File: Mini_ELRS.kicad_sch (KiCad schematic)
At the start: 24 parts, among them J1 Conn_01x06, J2 Conn_01x06, J3 Conn_01x06, SW1 SW_Push, U1 ESP32-PICO-D4, U2 TC2014-3.3VxCTTR, U3 SX1280IMLTRT, Y1 Crystal_GND24_Small

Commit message: update esp32_with_mos
Signed-off-by: huangzzk <huangcmzzk@gmail.com>
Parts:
- removed J1, J2, J3: Conn_01x06, Connector_PinHeader_2.54mm:PinHeader_1x06_P2.54mm_Vertical, symbol Connector_Generic:Conn_01x06
- added J1, J2, J4, J6: Conn_01x03_MountingPin, Connector_Molex:Molex_CLIK-Mate_502386-0370_1x03-1MP_P1.25mm_Horizontal, symbol Connector_Generic_MountingPin:Conn_01x03_MountingPin
- added J3: Conn_01x04, Connector_PinHeader_2.54mm:PinHeader_1x04_P2.54mm_Vertical, symbol Connector_Generic:Conn_01x04
- added J5: Conn_01x03, Connector_Molex:Molex_CLIK-Mate_502386-0370_1x03-1MP_P1.25mm_Horizontal, symbol Connector_Generic:Conn_01x03
- added Q1, Q2: Q_NMOS_GSD, Package_TO_SOT_SMD:SOT-23, symbol Device:Q_NMOS_GSD
- added R4, R5: 10K, Resistor_SMD:R_0402_1005Metric, symbol Device:R
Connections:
- net BUSY: now also U1.5 (SENSOR_VP); no longer U1.34 (IO5)
- net DIO1: now also U1.7 (SENSOR_CAPN); no longer U1.24 (IO4)
- net GND: now also J1.MP (MountPin), J2.MP (MountPin), J3.4 (Pin_4), J4.3 (Pin_3), J4.MP (MountPin), J5.3 (Pin_3), J6.3 (Pin_3), J6.MP (MountPin), Q1.2 (S), Q2.2 (S), R4.2, R5.2
- net LED: now also U1.22 (IO2); no longer U1.35 (IO18)
- net MISO: now also U1.8 (SENSOR_VN); no longer U1.18 (IO12)
- net MOSI: now also U1.16 (IO27); no longer U1.20 (IO13)
- net NRST: now also U1.24 (IO4); no longer U1.22 (IO2)
- net NSS: now also U1.20 (IO13); no longer U1.21 (IO15)
- net RX: now also J3.2 (Pin_2)
- net SCK: now also U1.18 (IO12); no longer U1.17 (IO14)
- net TX: now also J3.3 (Pin_3)
- net PWM5: now reaches U1.28 (SD2/IO9)
- net PWM5: now also J6.1 (Pin_1)
- net PWM7: now reaches U1.12 (IO32)
- net PWM4: now reaches U1.13 (IO33)
- net PWM4: now also J5.1 (Pin_1)
- net PWM3: now reaches U1.14 (IO25)
- net PWM3: now also J4.1 (Pin_1)
- net PWM6: now reaches U1.36 (IO23)
- net PWM1: now reaches U1.39 (IO22)
- net PWM1: now also J1.1 (Pin_1), Q1.1 (G), R4.1
- net PWM8: now reaches U1.42 (IO21)
- net +5V renamed +BATT
- net +BATT: now also J1.2 (Pin_2), J2.2 (Pin_2), J3.1 (Pin_1), J4.2 (Pin_2), J5.2 (Pin_2), J6.2 (Pin_2)
- new net: J2.3 (Pin_3), Q2.3 (D)
- new net: J1.3 (Pin_3), Q1.3 (D)
- new net PWM2: J2.1 (Pin_1), Q2.1 (G), R5.1, U1.34 (IO5)
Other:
- moved on the sheet: AE1, D2, FL1, R3

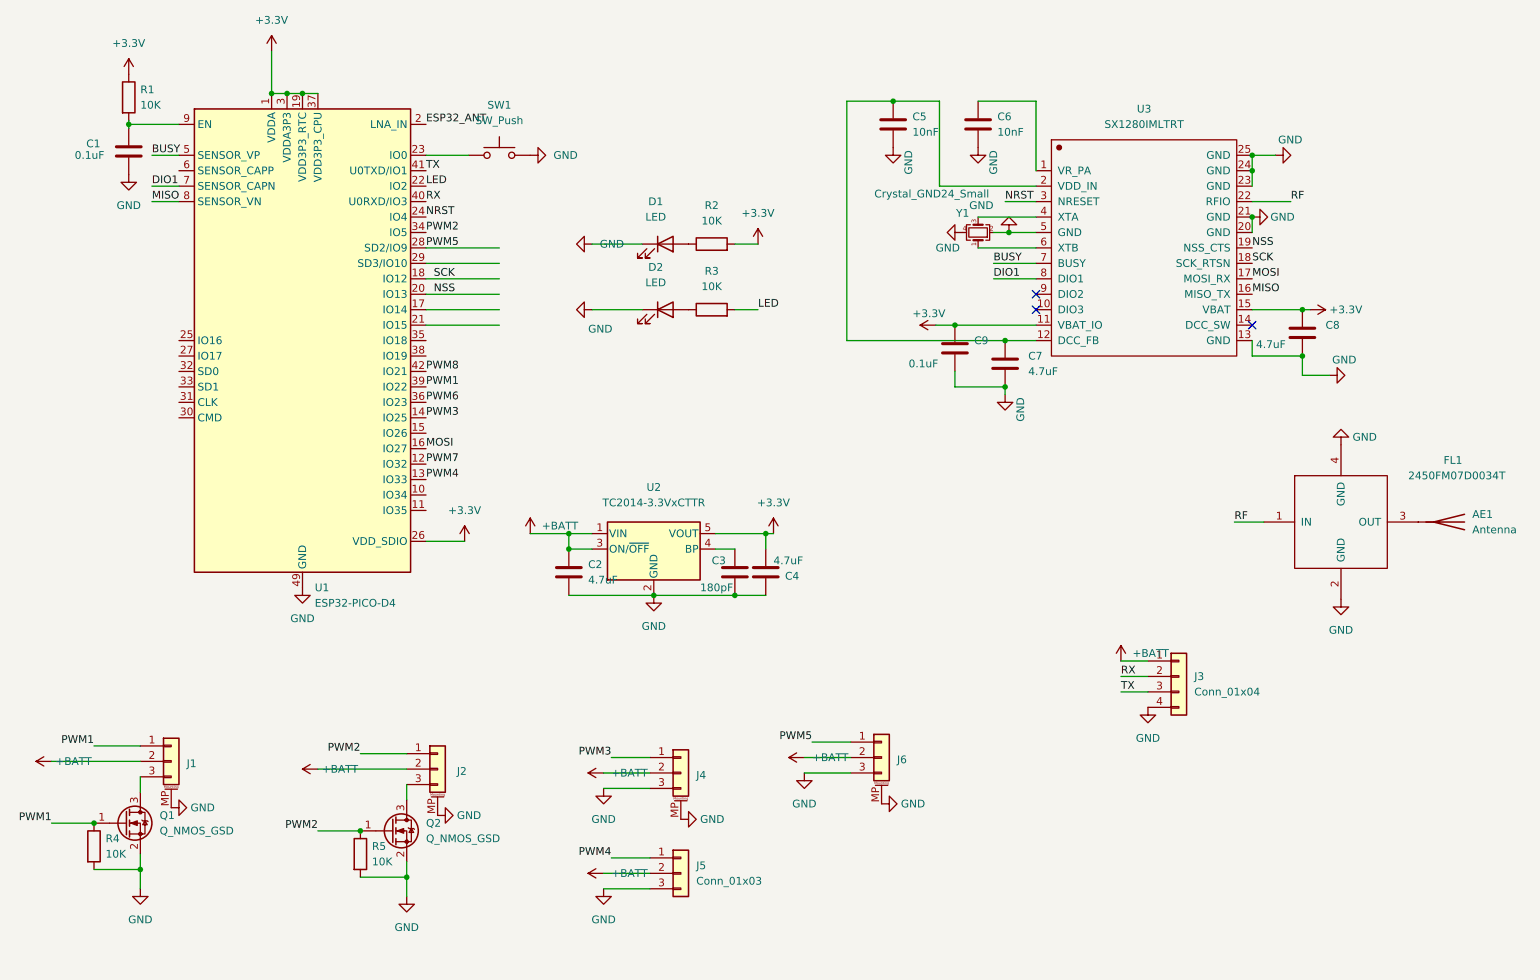
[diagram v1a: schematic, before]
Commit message: swap some pwm pins net name
Signed-off-by: huangzzk <huangcmzzk@gmail.com>
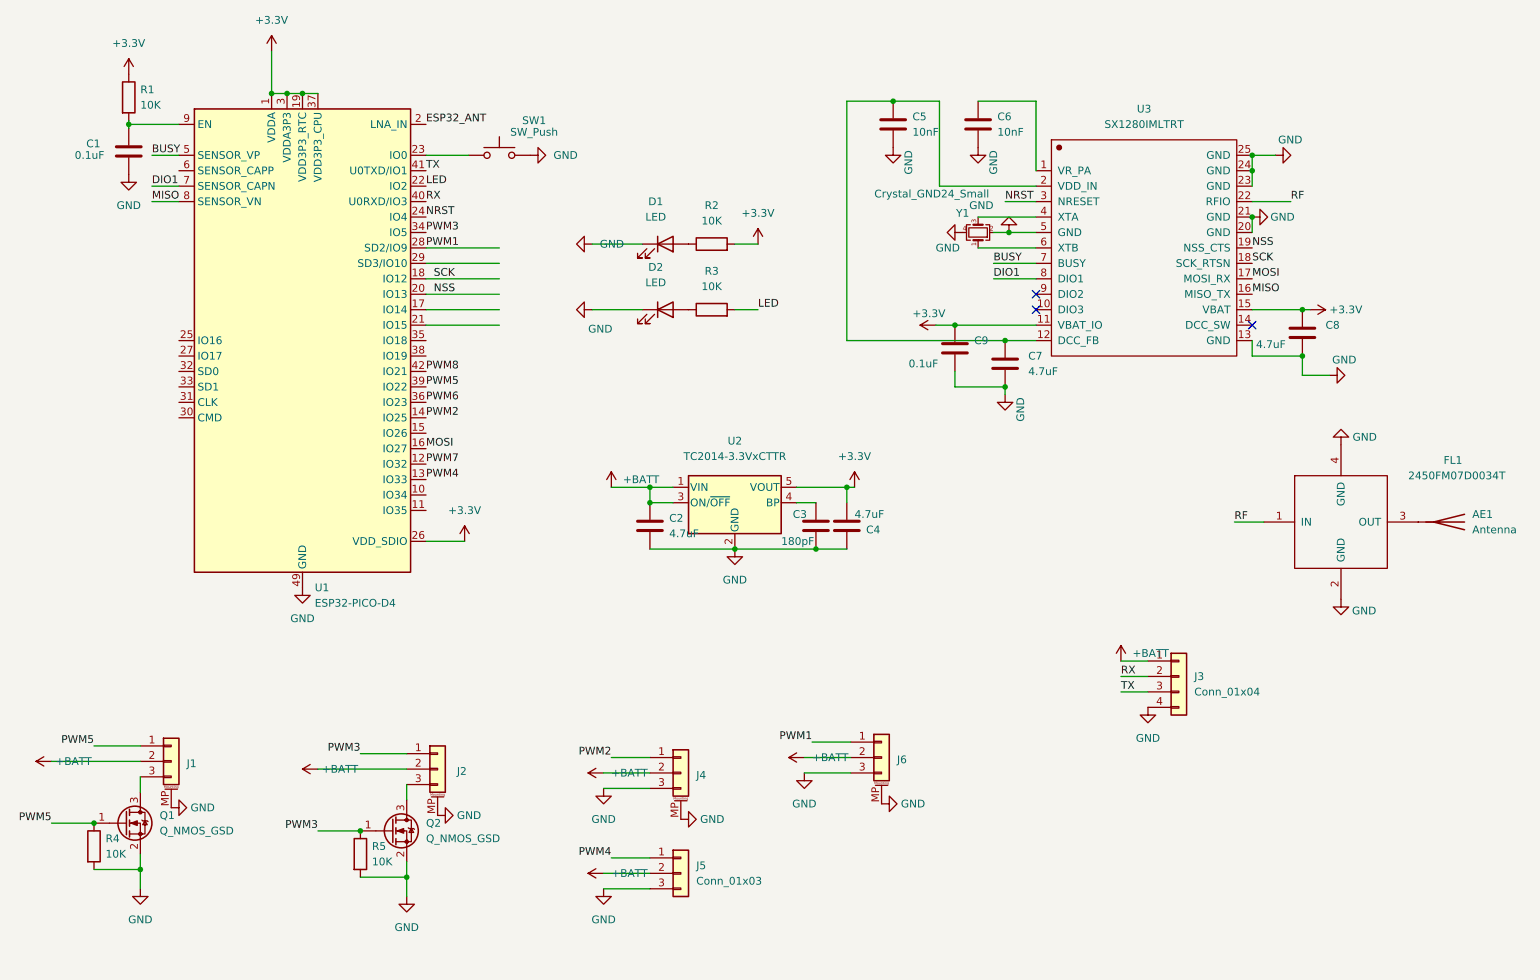
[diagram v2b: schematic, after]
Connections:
- net PWM1: now also J6.1 (Pin_1), U1.28 (SD2/IO9); no longer J1.1 (Pin_1), Q1.1 (G), R4.1, U1.39 (IO22)
- net PWM2: now also J4.1 (Pin_1), U1.14 (IO25); no longer J2.1 (Pin_1), Q2.1 (G), R5.1, U1.34 (IO5)
- net PWM3: now also J2.1 (Pin_1), Q2.1 (G), R5.1, U1.34 (IO5); no longer J4.1 (Pin_1), U1.14 (IO25)
- net PWM5: now also J1.1 (Pin_1), Q1.1 (G), R4.1, U1.39 (IO22); no longer J6.1 (Pin_1), U1.28 (SD2/IO9)
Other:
- moved on the sheet: C2, C3, C4, U2

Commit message: remove something unncessary
Signed-off-by: huangzzk <huangcmzzk@gmail.com>
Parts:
- removed D1: LED, LED_SMD:LED_0603_1608Metric, symbol Device:LED
- removed J1: Conn_01x03_MountingPin, Connector_Molex:Molex_CLIK-Mate_502386-0370_1x03-1MP_P1.25mm_Horizontal, symbol Connector_Generic_MountingPin:Conn_01x03_MountingPin
- removed J5: Conn_01x03, Connector_Molex:Molex_CLIK-Mate_502386-0370_1x03-1MP_P1.25mm_Horizontal, symbol Connector_Generic:Conn_01x03
- removed SW1: SW_Push, Button_Switch_SMD:SW_Push_SPST_NO_Alps_SKRK, symbol Switch:SW_Push
- added J1: Conn_01x02, Connector_PinHeader_2.54mm:PinHeader_2x01_P2.54mm_Vertical, symbol Connector_Generic:Conn_01x02
- added J5: Conn_01x03_MountingPin, Connector_Molex:Molex_CLIK-Mate_502386-0370_1x03-1MP_P1.25mm_Horizontal, symbol Connector_Generic_MountingPin:Conn_01x03_MountingPin
- added R6: 10K, Resistor_SMD:R_0603_1608Metric, symbol Device:R
- R2: value 10K -> NC
- R4, R5: footprint Resistor_SMD:R_0402_1005Metric -> Resistor_SMD:R_0603_1608Metric
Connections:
- net +3V3: no longer R2.2
- net +BATT: now also J1.1 (Pin_1), J5.2 (Pin_2)
- net GND: now also R2.2, J5.3 (Pin_3), J5.MP (MountPin), R6.2
- net NSS: now also R6.1
- net PWM4: now also J5.1 (Pin_1)
- net at Q1.3 (D): now also J1.2 (Pin_2)
- net at R2.1: now also U1.23 (IO0)
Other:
- moved on the sheet: D2, R3

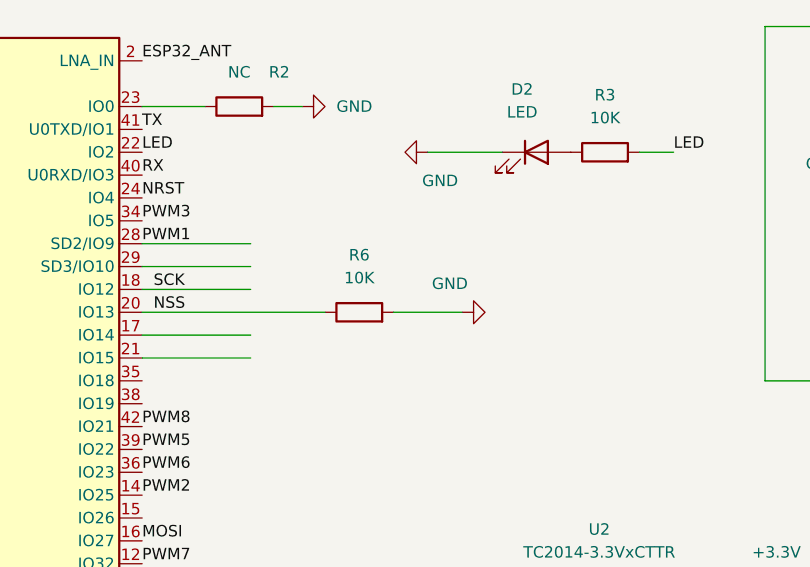
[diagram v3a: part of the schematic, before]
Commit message: finished pcb. using normal layer stack
Signed-off-by: huangzzk <huangcmzzk@gmail.com>
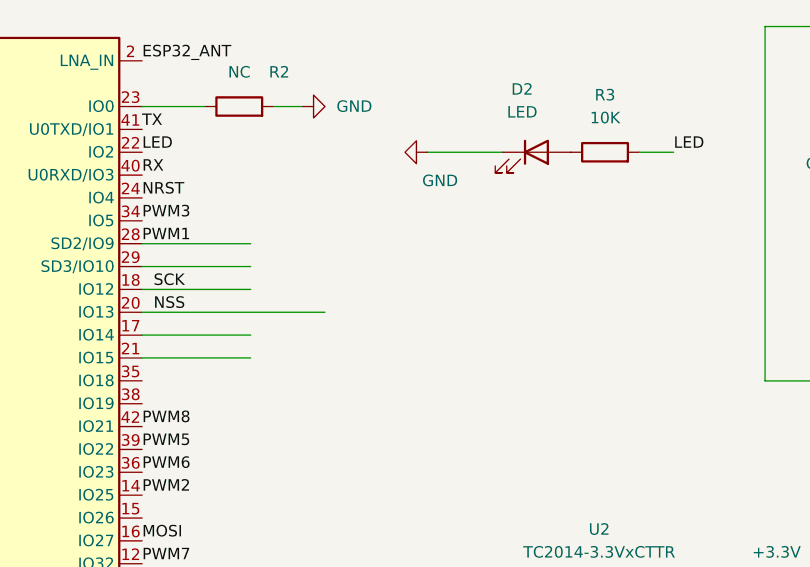
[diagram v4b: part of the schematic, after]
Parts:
- removed R6: 10K, Resistor_SMD:R_0603_1608Metric, symbol Device:R
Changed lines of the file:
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@@
   (no_connect (at 194.31 85.09))
   (no_connect (at 229.87 87.63))
-  (wire (pts (xy 129.54 82.55) (xy 121.92 82.55))
-    (stroke (width 0) (type default) (color 0 0 0 0))
-  )
   (wire (pts (xy 71.12 49.53) (xy 73.66 49.53))
     (stroke (width 0) (type default) (color 0 0 0 0))
@@
     (pin "1")
   )
-  (symbol (lib_id "Device:R") (at 118.11 82.55 90) (unit 1)
-    (in_bom yes) (on_board yes) (fields_autoplaced)
-    (property "Reference" "R6" (id 0) (at 118.11 76.2 90))
-    (property "Value" "10K" (id 1) (at 118.11 78.74 90))
-    (property "Footprint" "Resistor_SMD:R_0603_1608Metric" (id 2) (at 118.11 84.328 90)
-      (effects (font (size 1.27 1.27)) hide)
-    )
-    (property "Datasheet" "~" (id 3) (at 118.11 82.55 0)
-      (effects (font (size 1.27 1.27)) hide)
-    )
-    (pin "1")
-    (pin "2")
-  )
   (symbol (lib_id "power:GND") (at 125.73 64.77 270) (unit 1)
     (in_bom yes) (on_board yes)
@@
     (pin "3")
     (pin "MP")
-  )
-  (symbol (lib_id "power:GND") (at 129.54 82.55 90) (unit 1)
-    (in_bom yes) (on_board yes)
-    (property "Reference" "#PWR0114" (id 0) (at 135.89 82.55 0)
-      (effects (font (size 1.27 1.27)) hide)
-    )
-    (property "Value" "GND" (id 1) (at 130.175 79.375 90)
-      (effects (font (size 1.27 1.27)) (justify left))
-    )
-    (property "Footprint" "" (id 2) (at 129.54 82.55 0)
-      (effects (font (size 1.27 1.27)) hide)
-    )
-    (property "Datasheet" "" (id 3) (at 129.54 82.55 0)
-      (effects (font (size 1.27 1.27)) hide)
-    )
-    (pin "1")
   )
   (symbol (lib_id "RF_Module:ESP32-PICO-D4") (at 73.66 90.17 0) (unit 1)
@@
       (reference "#PWR0113") (unit 1) (value "+3.3V") (footprint "")
     )
-    (path "/b99f0ade-492b-4e95-b2d9-3cae4847f7c8"
-      (reference "#PWR0114") (unit 1) (value "GND") (footprint "")
-    )
     (path "/c424557c-de60-43fc-9d3b-22dc03bfab6a"
       (reference "#PWR0115") (unit 1) (value "+3.3V") (footprint "")
@@
       (reference "R5") (unit 1) (value "10K") (footprint "Resistor_SMD:R_0603_1608Metric")
     )
-    (path "/36107dd6-c0cf-486a-851d-353de8379728"
-      (reference "R6") (unit 1) (value "10K") (footprint "Resistor_SMD:R_0603_1608Metric")
-    )
     (path "/c07eebcc-30d2-439d-8030-faea6ade4486"

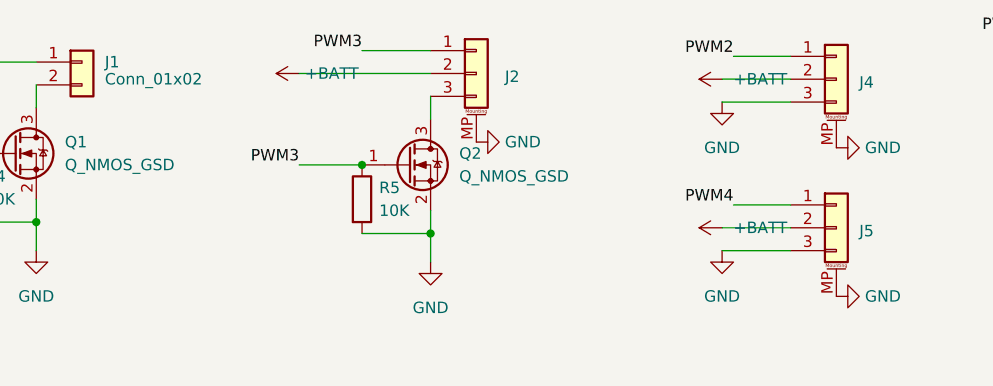
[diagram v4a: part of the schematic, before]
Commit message: edit the value of pulldown res of IO5
Signed-off-by: huangzzk <huangcmzzk@gmail.com>
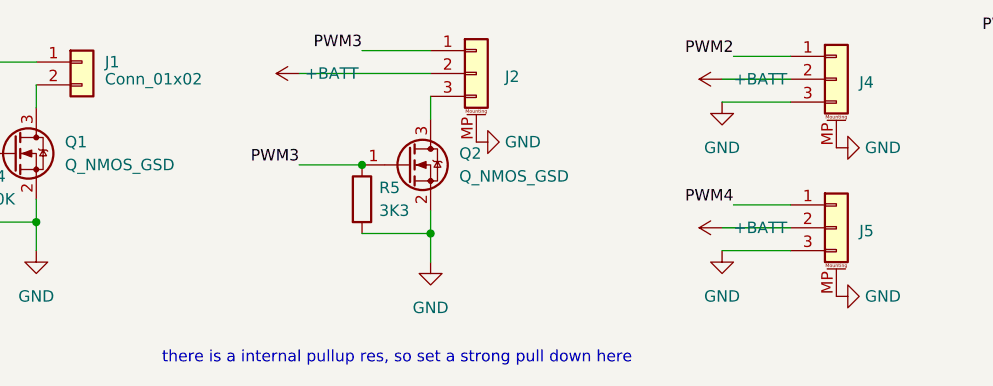
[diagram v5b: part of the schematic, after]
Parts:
- R5: value 10K -> 3K3
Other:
- note added: "there is a internal pullup res, so set a strong pull down here"
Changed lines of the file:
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@@
     (stroke (width 0) (type default) (color 0 0 0 0))
+  )
+  (text "there is a internal pullup res, so set a strong pull down here"
+    (at 60.96 193.04 0)
+    (effects (font (size 1.27 1.27)) (justify left bottom))
   )
   (label "RF" (at 226.949 120.015 0)
@@
       (effects (font (size 1.27 1.27)) (justify left))
     )
-    (property "Value" "10K" (id 1) (at 85.09 175.8949 0)
+    (property "Value" "3K3" (id 1) (at 85.09 175.8949 0)
       (effects (font (size 1.27 1.27)) (justify left))
     )
@@
     )
     (path "/1a039d88-7ab9-405d-bfaf-324c97ce2e32"
-      (reference "R5") (unit 1) (value "10K") (footprint "Resistor_SMD:R_0603_1608Metric")
+      (reference "R5") (unit 1) (value "3K3") (footprint "Resistor_SMD:R_0603_1608Metric")
     )
     (path "/c07eebcc-30d2-439d-8030-faea6ade4486"
